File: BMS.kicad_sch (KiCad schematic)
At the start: 50 parts, among them J1 Conn_01x05_Pin, J10 XT90PB-F, J11 XT90PB-F, J12 XT90PB-F, J2 XT90PB-F, J3 Conn_01x02_Pin, J4 Conn_01x03_Pin, J5 XT90PB-F, J6 XT90PB-F, J7 XT90PB-F, J8 XT90PB-F, J9 XT90PB-F, Q2 IRLB3813PBF, U1 BQ76920PW

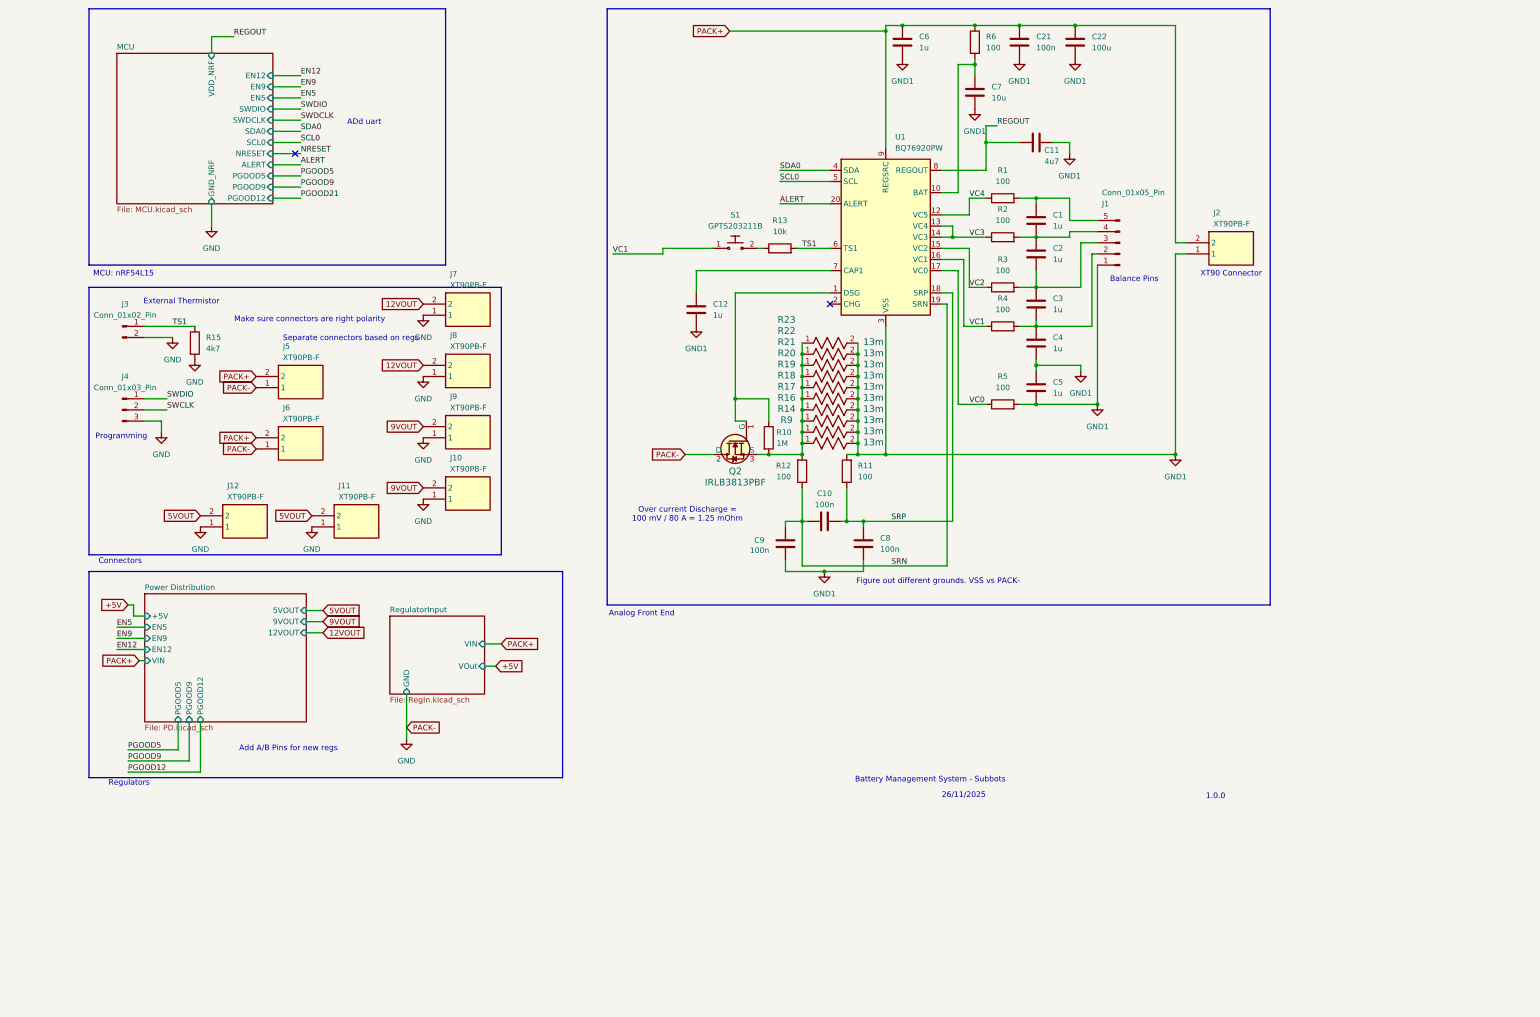
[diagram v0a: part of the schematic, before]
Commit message: Added A and Bonto the all the net labels and sheet outputs for the pairs of buck converters. Moved the XT90 connector for the battery input to the connectors sectionof the main sheet and renamed the nodes to BAT+ and BAT-. Added some comments clarifying the purpose of some connectors and which grounds go to which device.
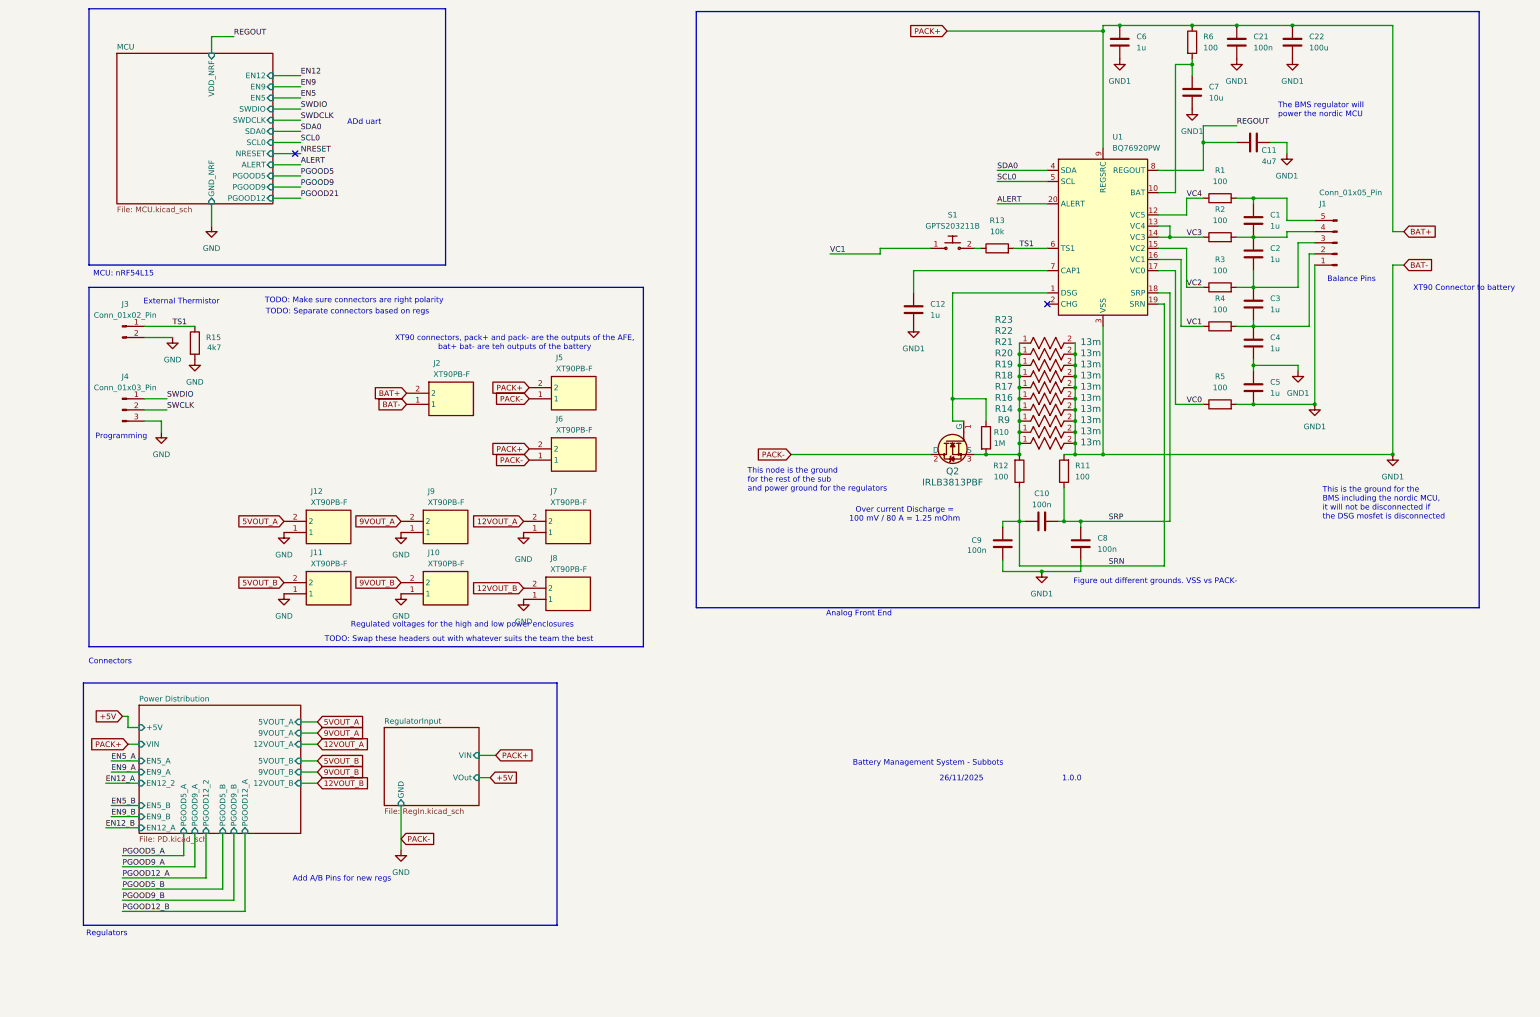
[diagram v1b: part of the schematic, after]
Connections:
- net 12VOUT renamed 12VOUT_A
- net 12VOUT_A: no longer J8.2
- net 5VOUT renamed 5VOUT_A
- net 5VOUT_A: no longer J11.2
- net 9VOUT renamed 9VOUT_A
- net 9VOUT_A: no longer J10.2
- net PACK+ renamed BAT+
- new net 12VOUT_B: J8.2
- new net 5VOUT_B: J11.2
- new net 9VOUT_B: J10.2
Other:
- sheet Power Distribution ports: added 12VOUT_A, 12VOUT_B, 5VOUT_A, 5VOUT_B, 9VOUT_A, 9VOUT_B, EN12_2, EN12_A, EN5_A, EN5_B, EN9_A, EN9_B, PGOOD12_2, PGOOD12_A, PGOOD5_A, PGOOD5_B, PGOOD9_A, PGOOD9_B; removed 12VOUT, 5VOUT, 9VOUT, EN12, EN5, EN9, PGOOD12, PGOOD5, PGOOD9 
- note added: "Regulated voltages for the high and low power enclosures"
- note added: "TODO: Make sure connectors are right polarity"
- note added: "TODO: Separate connectors based on regs"
- note added: "TODO: Swap these headers out with whatever suits the team the best"
- note added: "The BMS regulator will power the nordic MCU"
- note added: "This is the ground for the BMS including the nordic MCU, it will not be disconnected if the DSG mosfet is disconnected"
- note added: "This node is the ground for the rest of the sub and power ground for the regulators"
- note added: "XT90 Connector to battery"
- note added: "XT90 connectors, pack+ and pack- are the outputs of the AFE, bat+ bat- are teh outputs of the battery"
- note removed: "Make sure connectors are right polarity"
- note removed: "Separate connectors based on regs"
- note removed: "XT90 Connector"
- moved on the sheet: C1, C10, C11, C12, C2, C21, C22, C3, C4, C5, C6, C7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

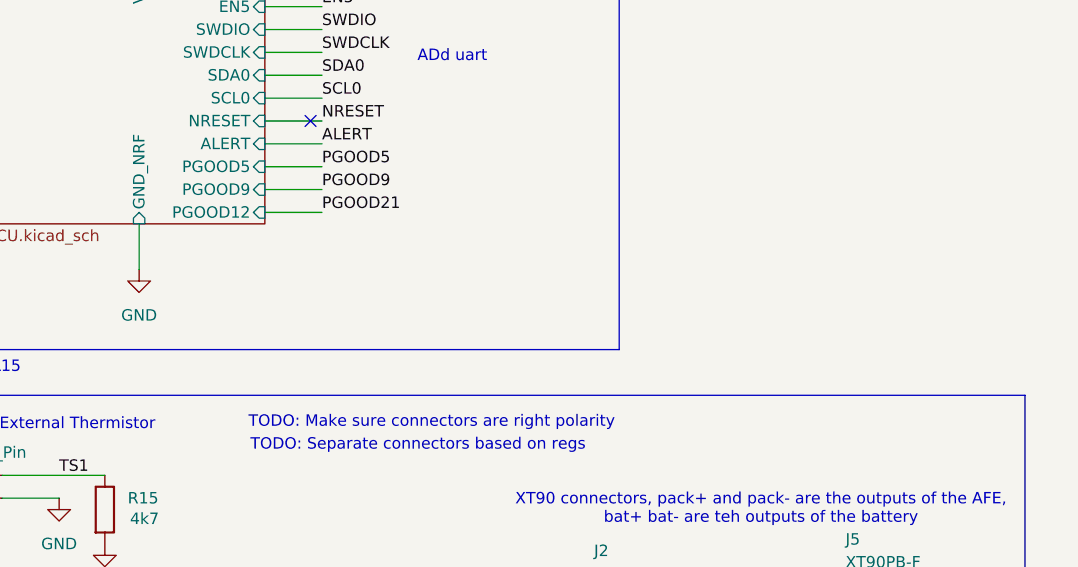
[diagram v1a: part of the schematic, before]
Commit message: Added note to change the ground of the Nordic MCU to the battery minus terminal rather than the ground of the rest of the sub. The power to the nordic won't be measured by coulomb counting, but I argue that this is negligable and the benifitis that the Nordic will not shut off in the event of an overcurrent, will change pending Hashaam's approval
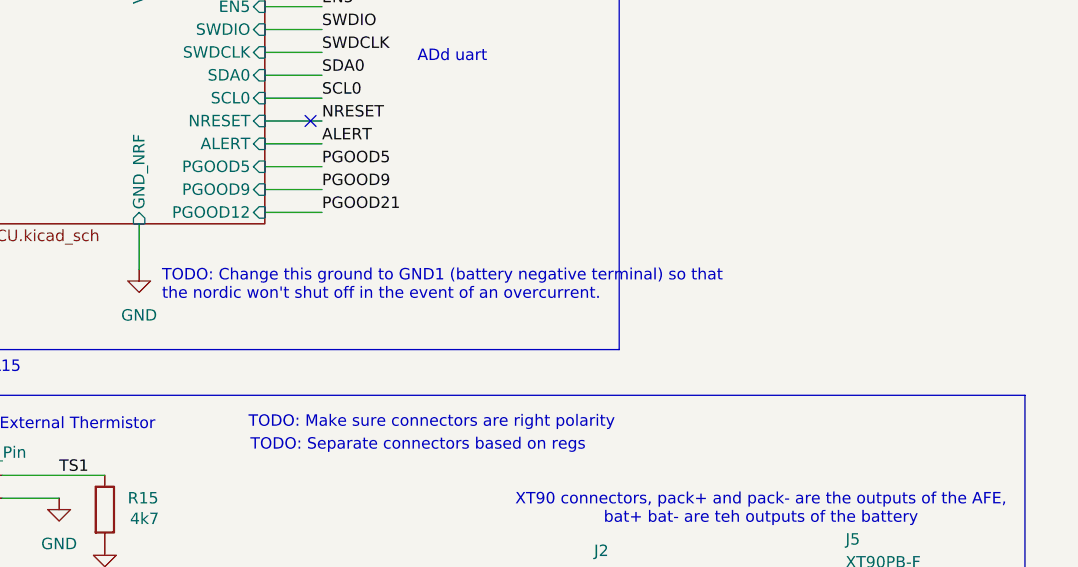
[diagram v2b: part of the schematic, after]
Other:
- note added: "TODO: Change this ground to GND1 (battery negative terminal) so that the nordic won't shut off in the event of an overcurrent."
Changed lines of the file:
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@@
+		)
+	)
+	(text "TODO: Change this ground to GND1 (battery negative terminal) so that\nthe nordic won't shut off in the event of an overcurrent."
+		(exclude_from_sim no)
+		(at 44.45 65.278 0)
+		(effects
+			(font
+				(size 1.27 1.27)
+			)
+			(justify left)
 		)
 	)

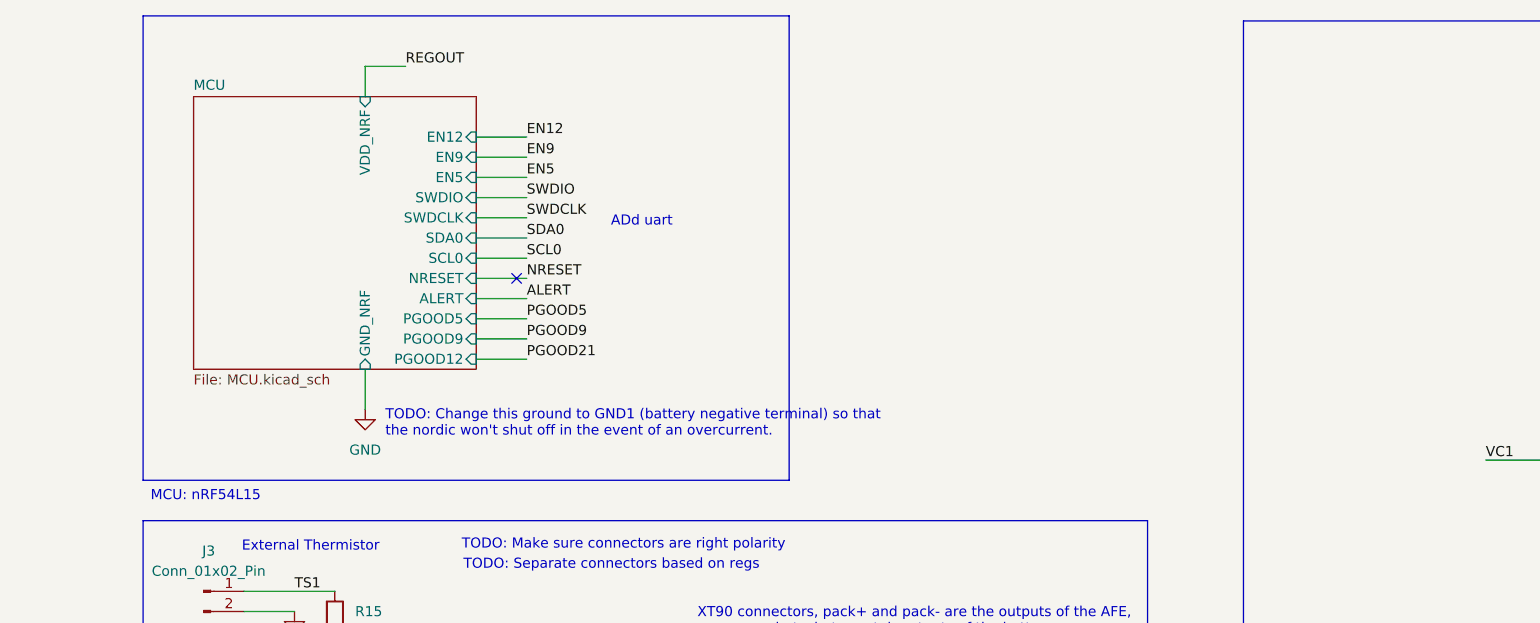
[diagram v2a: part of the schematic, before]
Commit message: Added EN and Pgood pins for the second set of buck converters to the NRF
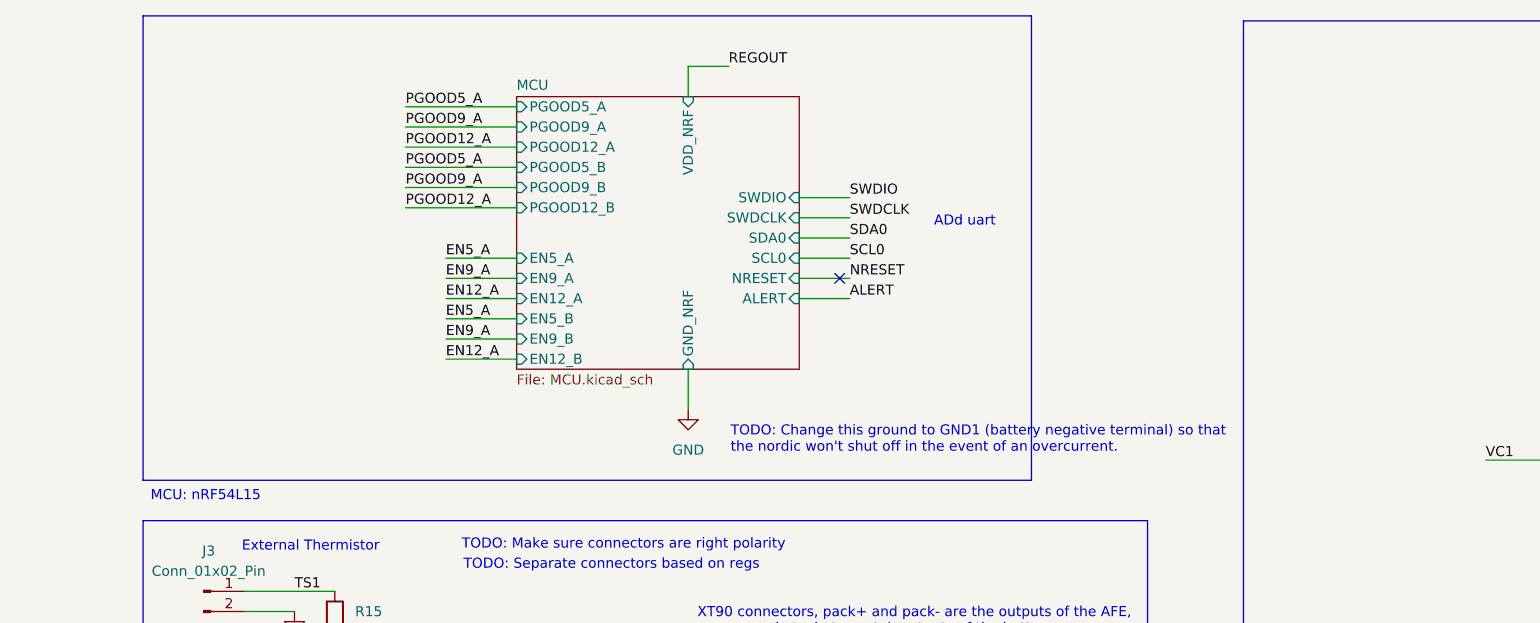
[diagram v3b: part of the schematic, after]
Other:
- sheet MCU ports: added EN12_A, EN12_B, EN5_A, EN5_B, EN9_A, EN9_B, PGOOD12_A, PGOOD12_B, PGOOD5_A, PGOOD5_B, PGOOD9_A, PGOOD9_B; removed EN12, EN5, EN9, PGOOD12, PGOOD5, PGOOD9

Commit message: dealing with merge issues
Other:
- note added: "Note: for 2oz copper and a 20cm temperature rise we can have 2cm thick pours, lets do that"
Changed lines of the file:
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@@
+		)
+	)
+	(text "Note: for 2oz copper and a 20cm temperature rise we can have 2cm thick pours, lets do that"
+		(exclude_from_sim no)
+		(at 219.964 169.672 0)
+		(effects
+			(font
+				(size 2.54 2.54)
+			)
 		)
 	)
